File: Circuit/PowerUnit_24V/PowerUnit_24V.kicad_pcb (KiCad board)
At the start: 2 copper layers, 100 x 76 mm, 54 parts, among them J1 Conn_01x02_Pin, J10 Conn_01x04_Pin, J12 Conn_01x02_Pin, J13 Conn_01x02_Pin, J19 Conn_01x02_Pin, J2 Conn_01x02_Pin, J3 Conn_01x02_Pin, J4 Conn_01x02_Pin, J5 Conn_01x02_Pin, J6 Conn_01x02_Pin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

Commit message: 24V基板完成
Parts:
- added G***: LOGO, OU_Picture:OkaLogo, B.Cu at (104.1, 81.3)
- moved R2 54.2 mm to (82.0, 33.4)
- moved C1 15.4 mm to (106.5, 43.2), turned to 180 degrees
- moved R3 12.9 mm to (108.3, 41.5), turned to 180 degrees
- moved C2 9.84 mm to (101.6, 39.2)
- moved C12 9.00 mm to (62.3, 25.0), turned to 90 degrees
- moved D3 8.89 mm to (101.8, 24.4), turned to 90 degrees
- moved C7 8.48 mm to (63.0, 29.4)
- moved J19 8.48 mm to (30.0, 46.7)
- moved R14 8.48 mm to (63.4, 40.4)
- moved D4 8.48 mm to (70.8, 37.1)
- moved D5 8.48 mm to (24.9, 84.1)
- moved J2 8.48 mm to (42.9, 90.5)
- moved J3 8.48 mm to (60.7, 90.5)
- moved J4 8.48 mm to (78.5, 90.5)
- moved J5 8.48 mm to (96.3, 90.5)
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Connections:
- D3 pad 1: GND -> GNDPWR
- J12 pad 2: Net-(J12-Pin_2) -> /Vsense1
- J13 pad 1: Net-(J12-Pin_2) -> /Vsense1
- J6 pad 1: GNDPWR -> GND
- J7 pad 1: GNDPWR -> GND
- J8 pad 1: GNDPWR -> GND
- J9 pad 1: GNDPWR -> GND
- K1 pad 87: Net-(J12-Pin_2) -> /Vsense1
- R3 pad 1: +24V_CTRL -> /Vsense1
- R5 pad 1: Net-(J12-Pin_2) -> /Vsense1
- R7 pad 1: Net-(J12-Pin_2) -> Net-(F1-Pad2)
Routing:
- net +3.3V: track 0.00 -> 64.3 mm
- net +24V_CTRL: track 0.00 -> 60.9 mm
- net /I2C_SCL: track 0.00 -> 44.7 mm
- net /I2C_SDA: track 0.00 -> 43.1 mm
- net Net-(K1-Pad30): track 0.00 -> 37.0 mm
- net +12V: track 0.00 -> 29.5 mm
- net /Vsense1: track 0.00 -> 27.3 mm
- net Net-(D4-K): track 0.00 -> 20.6 mm
- net Net-(J13-Pin_2): track 0.00 -> 17.5 mm
- net +24V_DRV: track 0.00 -> 15.9 mm
- net Net-(J19-Pin_2): track 0.00 -> 15.4 mm
- net Net-(F1-Pad2): track 0.00 -> 12.1 mm
- net Net-(Q1-D): track 0.00 -> 11.4 mm
- net Net-(K1-Pad87a): track 0.00 -> 10.2 mm
- net Net-(K3-Pad87a): track 0.00 -> 9.37 mm
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- added copper zone on B.Cu, net +24V_CTRL
- added copper zone on B.Cu, net +24V_DRV
- added copper zone on B.Cu, net /Vsense1
- added copper zone on B.Cu, net GND
- added copper zone on F.Cu, net GND
- added copper zone on B.Cu, net GNDPWR
- added copper zone on F.Cu, net GNDPWR
- added copper zone on B.Cu, net Net-(F1-Pad2)
- added copper zone on B.Cu, net Net-(J1-Pin_2)
- added copper zone on B.Cu, net Net-(K1-Pad30)
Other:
- board text added: "2026/06/19 Designed by E.Yoshioka"
- board text added: "24V INPUT"
- board text added: "24V基板"
- board text added: "3.3V"
- board text added: "BAT Voltage"
- board text added: "CTRL"
- board text added: "CTRL Power"
- board text added: "Current"
- board text added: "DRIVE"
- board text added: "DRIVE Power"
- board text added: "Delay Trim"
- board text added: "Emergency Switch"
- board text added: "GND"
- board text added: "Main Switch"
- board text added: "SCL"
- board text added: "SDA"
- board text added: "↻5.7s ↺0.24s"
- board text added: "岡山大学 ロボット研究会"

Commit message: メインモータ基板完成
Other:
- board text added: "2026/06/19 Designed by E.Yoshioka ver 1.0"
- board text added: "24V"
- board text added: "Board type:"
- board text removed: "2026/06/19 Designed by E.Yoshioka"
- board text removed: "24V基板"
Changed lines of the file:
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@@
 		(layer "Edge.Cuts")
+	)
+	(gr_text "Board type:"
+		(at 103.5 84.5 0)
+		(layer "F.SilkS")
+		(effects
+			(font
+				(size 1 1)
+				(thickness 0.2)
+				(bold yes)
+			)
+			(justify left)
+		)
 	)
 	(gr_text "Current"
@@
 		)
 	)
-	(gr_text "24V基板"
-		(at 104.14 87.63 0)
-		(layer "F.SilkS" knockout)
-		(effects
-			(font
-				(size 2.5 2.5)
-				(thickness 0.4)
-			)
-			(justify left bottom)
-		)
-	)
-	(gr_text "2026/06/19\nDesigned by E.Yoshioka"
-		(at 66.675 68.58 0)
+	(gr_text "24V"
+		(at 104 90.5 0)
+		(layer "F.SilkS" knockout)
+		(effects
+			(font
+				(face "Calibri")
+				(size 4 4)
+				(thickness 0.8)
+				(bold yes)
+			)
+			(justify left bottom)
+		)
+		(render_cache "24V" 0
+			(polygon
+				(pts
+					(xy 106.612177 89.529351) (xy 106.605338 89.663928) (xy 106.584822 89.755031) (xy 106.549162 89.805101)
+					(xy 106.500069 89.82) (xy 104.467236 89.82) (xy 104.363433 89.809253) (xy 104.292358 89.766999)
+					(xy 104.252791 89.675896) (xy 104.240579 89.520802) (xy 104.248639 89.367173) (xy 104.278681 89.253112)
+					(xy 104.334856 89.15517) (xy 104.423761 89.05039) (xy 105.035589 88.390935) (xy 105.207005 88.201504)
+					(xy 105.330635 88.043377) (xy 105.505512 87.757124) (xy 105.560027 87.628574) (xy 105.59173 87.518499)
+					(xy 105.614933 87.311137) (xy 105.586113 87.138213) (xy 105.550414 87.061453) (xy 105.50136 86.995819)
+					(xy 105.439085 86.942001) (xy 105.360676 86.900321) (xy 105.271492 86.874821) (xy 105.161374 86.865638)
+					(xy 105.005594 86.876386) (xy 104.875854 86.906427) (xy 104.657257 86.997285) (xy 104.499965 87.089364)
+					(xy 104.43913 87.122892) (xy 104.401779 87.131374) (xy 104.359281 87.11501) (xy 104.33046 87.060055)
+					(xy 104.312875 86.956985) (xy 104.306036 86.79896) (xy 104.310188 86.693203) (xy 104.3224 86.619197)
+					(xy 104.344382 86.564242) (xy 104.392009 86.507822) (xy 104.517794 86.426734) (xy 104.74323 86.332944)
+					(xy 105.038276 86.256008) (xy 105.20182 86.232678) (xy 105.374598 86.224745) (xy 105.640501 86.24323)
+					(xy 105.856734 86.294354) (xy 106.049184 86.379646) (xy 106.199651 86.488283) (xy 106.319051 86.624147)
+					(xy 106.403349 86.783084) (xy 106.453251 86.958513) (xy 106.470272 87.150181) (xy 106.462001 87.32125)
+					(xy 106.437299 87.488946) (xy 106.389039 87.656122) (xy 106.300767 87.848227) (xy 106.181846 88.042068)
+					(xy 106.008408 88.274187) (xy 105.801003 88.51359) (xy 105.508443 88.816406) (xy 105.095673 89.241632)
+					(xy 106.489323 89.241632) (xy 106.539637 89.257997) (xy 106.579448 89.308066) (xy 106.603872 89.397704)
+				)
+			)
+			(polygon
+				(pts
+					(xy 108.867271 86.278478) (xy 109.024319 86.300216) (xy 109.110537 86.336852) (xy 109.137892 86.388632)
+					(xy 109.137892 88.50695) (xy 109.452233 88.50695) (xy 109.489955 88.521378) (xy 109.527215 88.574605)
+					(xy 109.549222 88.653566) (xy 109.558722 88.79882) (xy 109.550365 88.930527) (xy 109.529902 89.012288)
+					(xy 109.493532 89.069459) (xy 109.452233 89.085317) (xy 109.137892 89.085317) (xy 109.137892 89.72621)
+					(xy 109.121528 89.774082) (xy 109.064131 89.808276) (xy 108.957397 89.828792) (xy 108.788136 89.835631)
+					(xy 108.622784 89.828792) (xy 108.51605 89.808276) (xy 108.461339 89.774082) (xy 108.446441 89.72621)
+					(xy 108.446441 89.085317) (xy 107.094068 89.085317) (xy 107.02568 89.075792) (xy 106.975122 89.031828)
+					(xy 106.94508 88.932909) (xy 106.935554 88.760963) (xy 106.939706 88.608555) (xy 106.95161 88.50695)
+					(xy 107.509281 88.50695) (xy 108.446441 88.50695) (xy 108.446441 86.896901) (xy 108.441067 86.896901)
+					(xy 107.509281 88.50695) (xy 106.95161 88.50695) (xy 106.953384 88.491807) (xy 106.980495 88.392889)
+					(xy 107.02568 88.29397) (xy 108.12404 86.366894) (xy 108.170446 86.32464) (xy 108.262037 86.294842)
+					(xy 108.411025 86.277257) (xy 108.629623 86.271639)
+				)
+			)
+			(polygon
+				(pts
+					(xy 111.81919 89.693726) (xy 111.783531 89.768953) (xy 111.712456 89.812428) (xy 111.578611 89.831479)
+					(xy 111.357571 89.835631) (xy 111.170237 89.834166) (xy 111.037857 89.827327) (xy 110.948953 89.811207)
+					(xy 110.891556 89.783852) (xy 110.85614 89.744284) (xy 110.832937 89.685422) (xy 109.780739 86.55545)
+					(xy 109.741172 86.399867) (xy 109.745091 86.348155) (xy 109.768527 86.313893) (xy 109.809958 86.292238)
+					(xy 109.884542 86.278478) (xy 110.114131 86.271639) (xy 110.31099 86.277257) (xy 110.420167 86.296308)
+					(xy 110.473412 86.337096) (xy 110.502233 86.40524) (xy 111.362944 89.128792) (xy 111.365631 89.128792)
+					(xy 112.209979 86.418918) (xy 112.237334 86.343935) (xy 112.293265 86.298995) (xy 112.406838 86.277257)
+					(xy 112.609071 86.271639) (xy 112.804221 86.279944) (xy 112.86654 86.29535) (xy 112.899965 86.319511)
+					(xy 112.916585 86.355184) (xy 112.916329 86.408171) (xy 112.874075 86.560823)
+				)
+			)
+		)
+	)
+	(gr_text "2026/06/19\nDesigned by E.Yoshioka\n\nver 1.0"
+		(at 66.5 64.5 0)
 		(layer "B.SilkS")
 		(effects
@@
 				(bold yes)
 			)
-			(justify left bottom mirror)
-		)
-	)
+			(justify left top mirror)
+		)
+	)

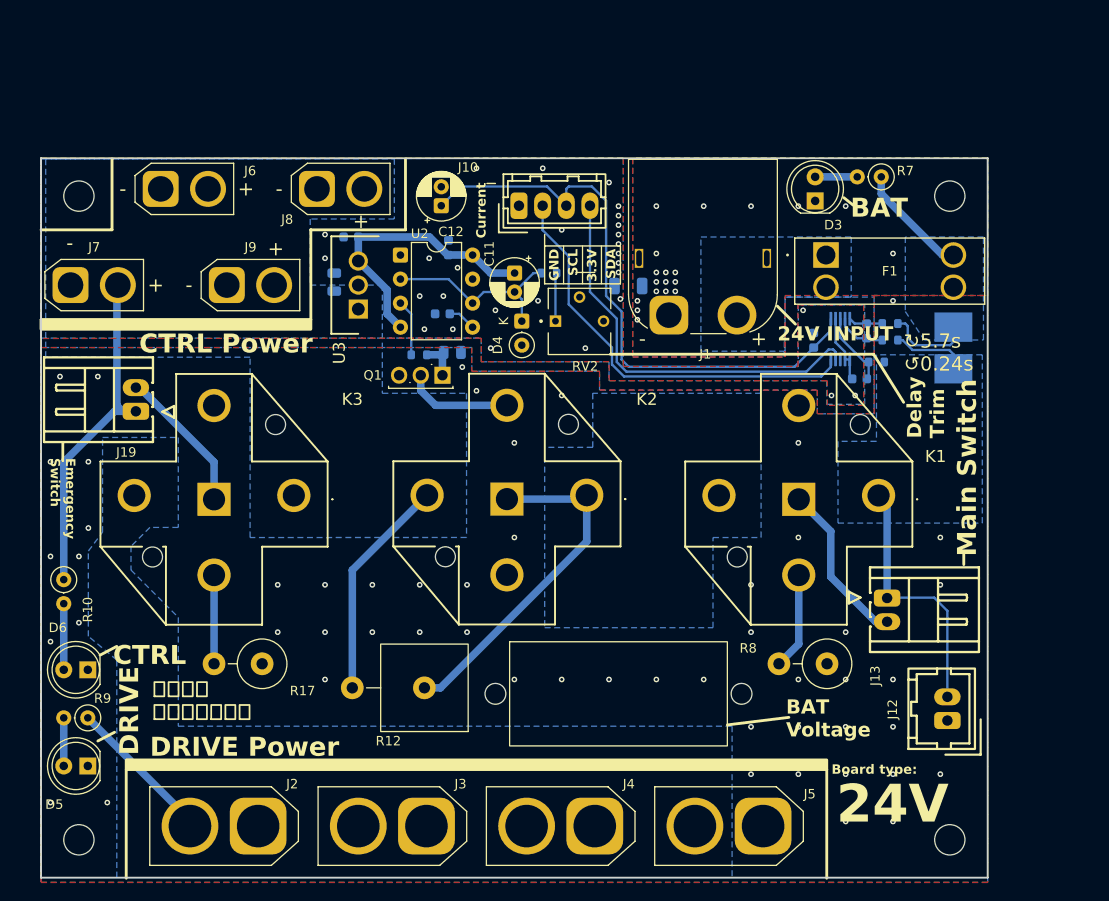
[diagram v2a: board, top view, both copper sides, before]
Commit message: 24V基板とメインモータ基板を修正
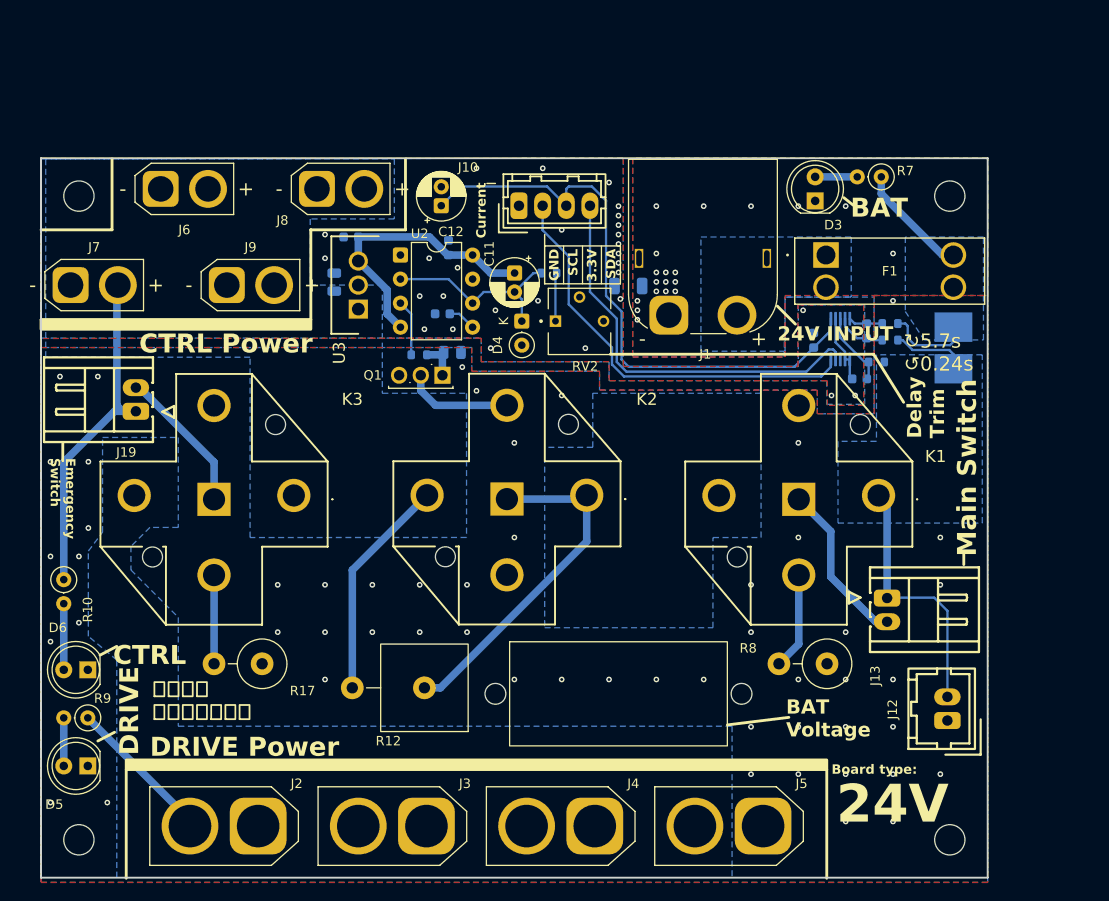
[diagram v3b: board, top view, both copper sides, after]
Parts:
- J2, J3, J4, J5: footprint Connector_AMASS:AMASS_XT60-M_1x02_P7.20mm_Vertical -> OU_Conn:AMASS_XT60-F
- J6, J7, J8, J9: footprint OU_Conn:XT30U-M -> OU_Conn:AMASS_XT30U-F
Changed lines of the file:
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@@
 		)
 	)
-	(footprint "OU_Conn:XT30U-M"
+	(footprint "OU_Conn:AMASS_XT30U-F"
 		(layer "F.Cu")
 		(at 23.115 33.335)
-		(descr "Connector XT30 Vertical Cable Male, https://www.tme.eu/Document/7d9d972ae3468777f69ec2ee99897652/XT30U-M.pdf")
+		(descr "Connector XT30 Vertical Cable Female, https://www.tme.eu/Document/f2d0830114aabe6ea8d4bb128e962790/XT30U-F.pdf")
 		(tags "RC Connector XT30")
 		(property "Reference" "J7"
@@
 		)
 		(fp_text user "-"
-			(at -0.08 -4.445 0)
+			(at -4 0 0)
 			(layer "F.SilkS")
 			(effects
@@
 		(pad "2" thru_hole circle
 			(at 5 0)
-			(size 3.8 3.8)
+			(size 4 4)
 			(drill 2.7)
 			(layers "*.Cu" "*.Mask")
@@
 		)
 		(embedded_fonts no)
-		(model "${KIPRJMOD}/libs/3Dmodels/XT30U-M.stp"
+		(model "${KIPRJMOD}/libs/3Dmodels/XT30U-F.step"
 			(offset
-				(xyz 8 4 38)
+				(xyz 2.5 0 0)
 			)
 			(scale
@@
 			)
 			(rotate
-				(xyz 90 -0 -0)
+				(xyz -180 -0 -180)
 			)
 		)
@@
 		)
 	)
-	(footprint "OU_Conn:XT30U-M"
+	(footprint "OU_Conn:AMASS_XT30U-F"
 		(layer "F.Cu")
 		(at 49.15 23.175)
-		(descr "Connector XT30 Vertical Cable Male, https://www.tme.eu/Document/7d9d972ae3468777f69ec2ee99897652/XT30U-M.pdf")
+		(descr "Connector XT30 Vertical Cable Female, https://www.tme.eu/Document/f2d0830114aabe6ea8d4bb128e962790/XT30U-F.pdf")
 		(tags "RC Connector XT30")
 		(property "Reference" "J8"
-			(at -3.15 3.225 0)
+			(at -3.65 3.325 0)
 			(layer "F.SilkS")
 			(effects
@@
 		)
 		(fp_text user "+"
-			(at 4.65 3.425 0)
+			(at 9 0 0)
 			(layer "F.SilkS")
 			(effects
@@
 		(pad "2" thru_hole circle
 			(at 5 0)
-			(size 3.8 3.8)
+			(size 4 4)
 			(drill 2.7)
 			(layers "*.Cu" "*.Mask")
@@
 		)
 		(embedded_fonts no)
-		(model "${KIPRJMOD}/libs/3Dmodels/XT30U-M.stp"
+		(model "${KIPRJMOD}/libs/3Dmodels/XT30U-F.step"
 			(offset
-				(xyz 8 4 38)
+				(xyz 2.5 0 0)
 			)
 			(scale
@@
 			)
 			(rotate
-				(xyz 90 -0 -0)
+				(xyz -180 -0 -180)
 			)
 		)
@@
 		)
 	)
-	(footprint "Connector_AMASS:AMASS_XT60-M_1x02_P7.20mm_Vertical"
+	(footprint "OU_Conn:AMASS_XT60-F"
 		(layer "F.Cu")
 		(at 42.935 90.485 180)
@@
 		(tags "XT60 female vertical")
 		(property "Reference" "J2"
-			(at -3.595 4.445 0)
+			(at -4.065 4.485 0)
 			(layer "F.SilkS")
 			(effects
@@
 		)
 		(property "Value" "Conn_01x02_Pin"
-			(at 3.6 5.4 0)
+			(at 3.6 5.4 180)
 			(layer "F.Fab")
 			(effects
@@
 		)
 		(fp_text user "${REFERENCE}"
-			(at 3.6 0.05 0)
+			(at 3.6 0.05 180)
 			(layer "F.Fab")
 			(effects
@@
 		)
 		(embedded_fonts no)
-		(model "${KICAD10_3DMODEL_DIR}/Connector_AMASS.3dshapes/AMASS_XT60-M_1x02_P7.2mm_Vertical.step"
+		(model "${KIPRJMOD}/libs/3Dmodels/XT60-F--3DModel-STEP-510211.STEP"
 			(offset
-				(xyz 0 0 0)
+				(xyz 3.5 0 0)
 			)
 			(scale
@@
 			)
 			(rotate
-				(xyz 0 0 0)
+				(xyz -90 -0 -180)
 			)
 		)
@@
 		(embedded_fonts no)
 	)
-	(footprint "Connector_AMASS:AMASS_XT60-M_1x02_P7.20mm_Vertical"
+	(footprint "OU_Conn:AMASS_XT60-F"
 		(layer "F.Cu")
 		(at 96.275 90.485 180)
@@
 		(tags "XT60 female vertical")
 		(property "Reference" "J5"
-			(at -4.925 3.385 0)
+			(at -4.065 4.485 0)
 			(layer "F.SilkS")
 			(effects
@@
 		)
 		(embedded_fonts no)
-		(model "${KICAD10_3DMODEL_DIR}/Connector_AMASS.3dshapes/AMASS_XT60-M_1x02_P7.2mm_Vertical.step"
+		(model "${KIPRJMOD}/libs/3Dmodels/XT60-F--3DModel-STEP-510211.STEP"
 			(offset
-				(xyz 0 0 0)
+				(xyz 3.5 0 0)
 			)
 			(scale
@@
 			)
 			(rotate
-				(xyz 0 0 0)
+				(xyz -90 -0 -180)
 			)
 		)
@@
 		)
 	)
-	(footprint "Connector_AMASS:AMASS_XT60-M_1x02_P7.20mm_Vertical"
+	(footprint "OU_Conn:AMASS_XT60-F"
 		(layer "F.Cu")
 		(at 60.715 90.485 180)
@@
 		(tags "XT60 female vertical")
 		(property "Reference" "J3"
-			(at -3.595 4.445 0)
+			(at -4.065 4.485 0)
 			(layer "F.SilkS")
 			(effects
@@
 		)
 		(property "Value" "Conn_01x02_Pin"
-			(at 3.6 5.4 0)
+			(at 3.6 5.4 180)
 			(layer "F.Fab")
 			(effects
@@
 		)
 		(fp_text user "${REFERENCE}"
-			(at 3.6 0.05 0)
+			(at 3.6 0.05 180)
 			(layer "F.Fab")
 			(effects
@@
 		)
 		(embedded_fonts no)
-		(model "${KICAD10_3DMODEL_DIR}/Connector_AMASS.3dshapes/AMASS_XT60-M_1x02_P7.2mm_Vertical.step"
+		(model "${KIPRJMOD}/libs/3Dmodels/XT60-F--3DModel-STEP-510211.STEP"
 			(offset
-				(xyz 0 0 0)
+				(xyz 3.5 0 0)
 			)
 			(scale
@@
 			)
 			(rotate
-				(xyz 0 0 0)
+				(xyz -90 -0 -180)
 			)
 		)
@@
 		)
 	)
-	(footprint "Connector_AMASS:AMASS_XT60-M_1x02_P7.20mm_Vertical"
+	(footprint "OU_Conn:AMASS_XT60-F"
 		(layer "F.Cu")
 		(at 78.495 90.485 180)
@@
 		(tags "XT60 female vertical")
 		(property "Reference" "J4"
-			(at -3.595 4.445 0)
+			(at -4.065 4.485 0)
 			(layer "F.SilkS")
 			(effects
@@
 		)
 		(property "Value" "Conn_01x02_Pin"
-			(at 3.6 5.4 0)
+			(at 3.6 5.4 180)
 			(layer "F.Fab")
 			(effects
@@
 		)
 		(fp_text user "${REFERENCE}"
-			(at 3.6 0.05 0)
+			(at 3.6 0.05 180)
 			(layer "F.Fab")
 			(effects
@@
 		)
 		(embedded_fonts no)
-		(model "${KICAD10_3DMODEL_DIR}/Connector_AMASS.3dshapes/AMASS_XT60-M_1x02_P7.2mm_Vertical.step"
+		(model "${KIPRJMOD}/libs/3Dmodels/XT60-F--3DModel-STEP-510211.STEP"
 			(offset
-				(xyz 0 0 0)
+				(xyz 3.5 0 0)
 			)
 			(scale
@@
 			)
 			(rotate
-				(xyz 0 0 0)
+				(xyz -90 -0 -180)
 			)
 		)
@@
 		)
 	)
-	(footprint "OU_Conn:XT30U-M"
+	(footprint "OU_Conn:AMASS_XT30U-F"
 		(layer "F.Cu")
 		(at 32.64 23.175)
-		(descr "Connector XT30 Vertical Cable Male, https://www.tme.eu/Document/7d9d972ae3468777f69ec2ee99897652/XT30U-M.pdf")
+		(descr "Connector XT30 Vertical Cable Female, https://www.tme.eu/Document/f2d0830114aabe6ea8d4bb128e962790/XT30U-F.pdf")
 		(tags "RC Connector XT30")
 		(property "Reference" "J6"
-			(at 9.445 -1.905 0)
+			(at 2.5 4.325 0)
 			(layer "F.SilkS")
 			(effects
@@
 		(pad "2" thru_hole circle
 			(at 5 0)
-			(size 3.8 3.8)
+			(size 4 4)
 			(drill 2.7)
 			(layers "*.Cu" "*.Mask")
@@
 		)
 		(embedded_fonts no)
-		(model "${KIPRJMOD}/libs/3Dmodels/XT30U-M.stp"
+		(model "${KIPRJMOD}/libs/3Dmodels/XT30U-F.step"
 			(offset
-				(xyz 8 4 38)
+				(xyz 2.5 0 0)
 			)
 			(scale
@@
 			)
 			(rotate
-				(xyz 90 -0 -0)
+				(xyz -180 -0 -180)
 			)
 		)
 	)
-	(footprint "OU_Conn:XT30U-M"
+	(footprint "OU_Conn:AMASS_XT30U-F"
 		(layer "F.Cu")
 		(at 39.625 33.335)
-		(descr "Connector XT30 Vertical Cable Male, https://www.tme.eu/Document/7d9d972ae3468777f69ec2ee99897652/XT30U-M.pdf")
+		(descr "Connector XT30 Vertical Cable Female, https://www.tme.eu/Document/f2d0830114aabe6ea8d4bb128e962790/XT30U-F.pdf")
 		(tags "RC Connector XT30")
 		(property "Reference" "J9"
@@
 		)
 		(fp_text user "+"
-			(at 5.175 -3.835 0)
+			(at 9 0 0)
 			(layer "F.SilkS")
 			(effects
@@
 		(pad "2" thru_hole circle
 			(at 5 0)
-			(size 3.8 3.8)
+			(size 4 4)
 			(drill 2.7)
 			(layers "*.Cu" "*.Mask")
@@
 		)
 		(embedded_fonts no)
-		(model "${KIPRJMOD}/libs/3Dmodels/XT30U-M.stp"
+		(model "${KIPRJMOD}/libs/3Dmodels/XT30U-F.step"
 			(offset
-				(xyz 8 4 38)
+				(xyz 2.5 0 0)
 			)
 			(scale
@@
 			)
 			(rotate
-				(xyz 90 -0 -0)
+				(xyz -180 -0 -180)
 			)
 		)
@@
 		(stroke
 			(width 0.1)
-			(type default)
-		)
-		(layer "F.SilkS")
-	)
-	(gr_line
-		(start 78.5 32)
-		(end 76.5 32)
-		(stroke
-			(width 0.1)

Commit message: YDS512F基板完成 24V基板とメインモータ基板を微修正
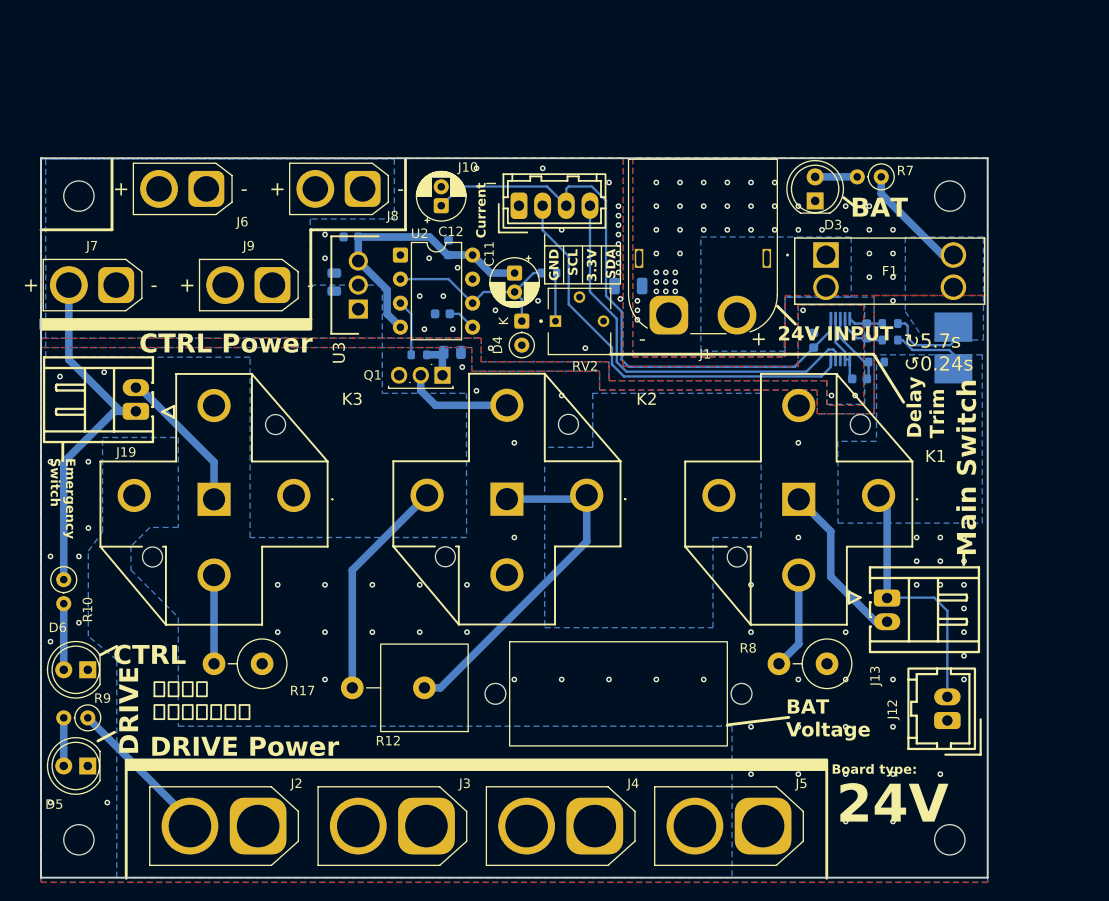
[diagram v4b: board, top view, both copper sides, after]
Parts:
- moved J6 4.83 mm to (37.5, 23.2), turned to 180 degrees
- moved J7 4.83 mm to (27.9, 33.3), turned to 180 degrees
- moved J8 4.83 mm to (54.0, 23.2), turned to 180 degrees
- moved J9 4.83 mm to (44.5, 33.3), turned to 180 degrees
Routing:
- net +24V_CTRL: track 60.9 -> 63.1 mm
- net GNDPWR: vias 73 -> 109

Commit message: サーボ基板完成
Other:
- board text added: "ID:0"
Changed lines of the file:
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@@
 		(tags "connector Hirose DF13 vertical")
 		(property "Reference" "J10"
-			(at -5.386 -4.053 0)
+			(at -0.986 4.547 0)
 			(layer "F.SilkS")
 			(effects
@@
 		)
 	)
+	(gr_text "ID:0"
+		(at 67.3 21.2 0)
+		(layer "F.SilkS" knockout)
+		(effects
+			(font
+				(size 1 1)
+				(thickness 0.2)
+				(bold yes)
+			)
+			(justify right)
+		)
+	)
